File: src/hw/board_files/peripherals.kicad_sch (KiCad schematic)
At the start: 28 parts, among them J5 Molex 104031-0811, Q1 PMOS, U5 NHD-C0220BIZ-FSRGB, U6 NEO-M9N, U7 BQ27427, U8 SHT30-DIS

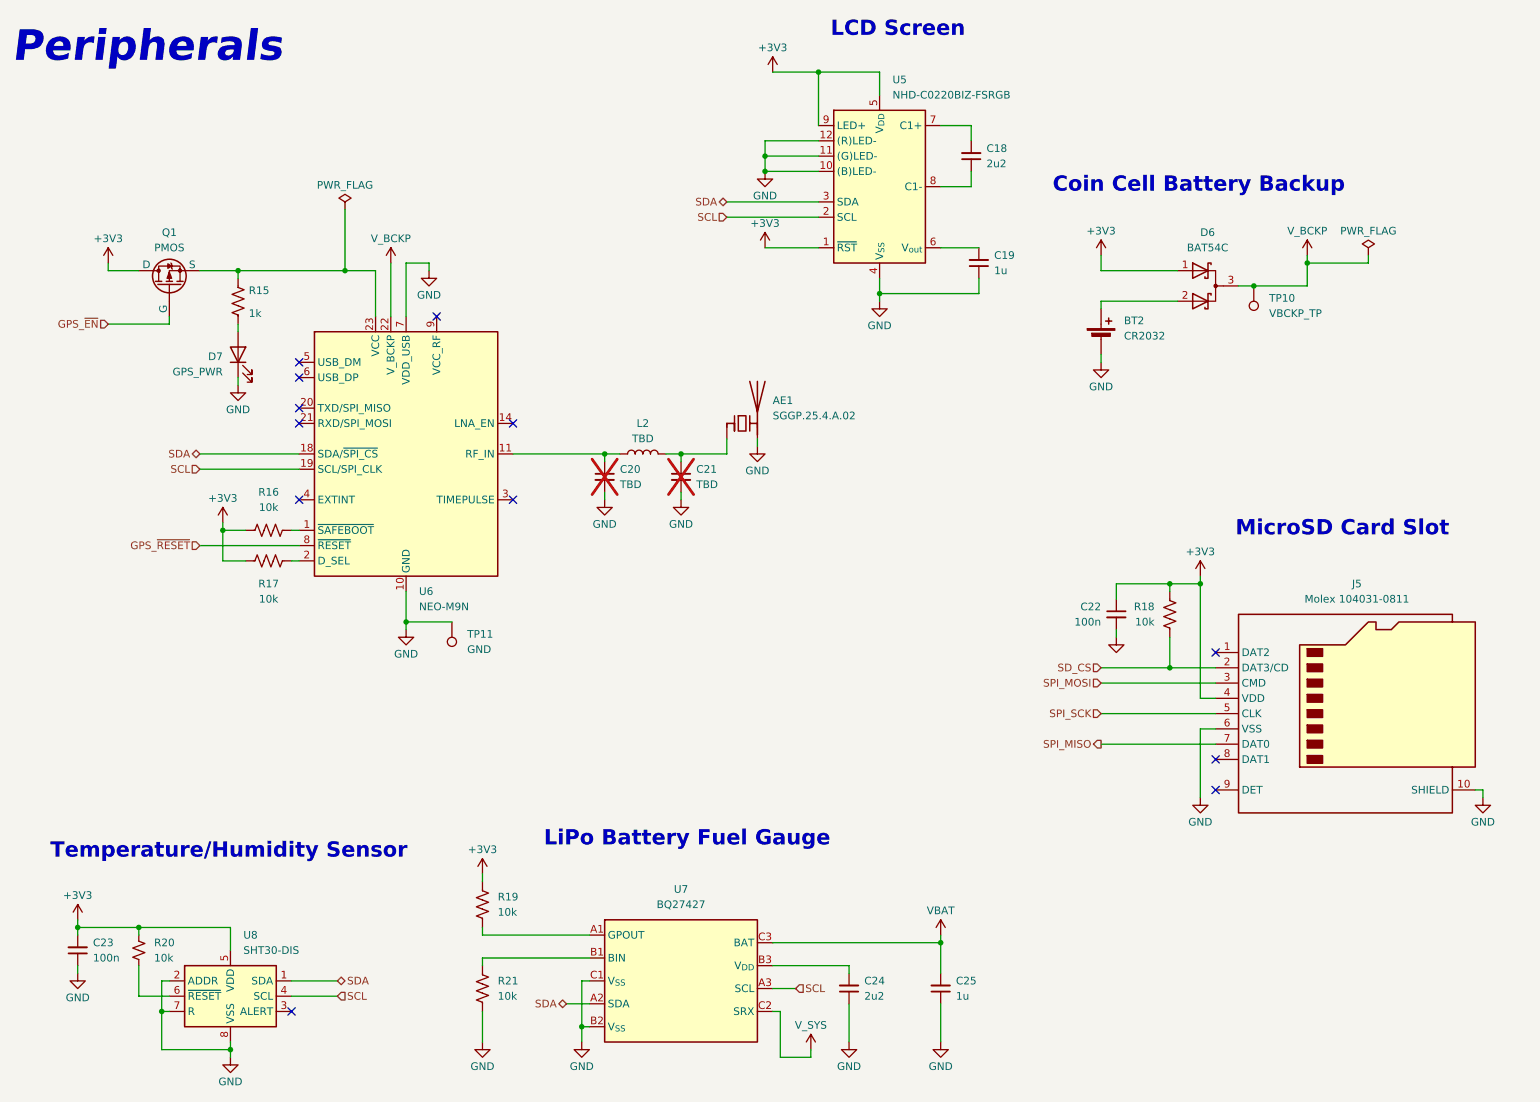
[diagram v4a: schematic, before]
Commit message: Lots of layout progress, changed some references (need to update BOM)
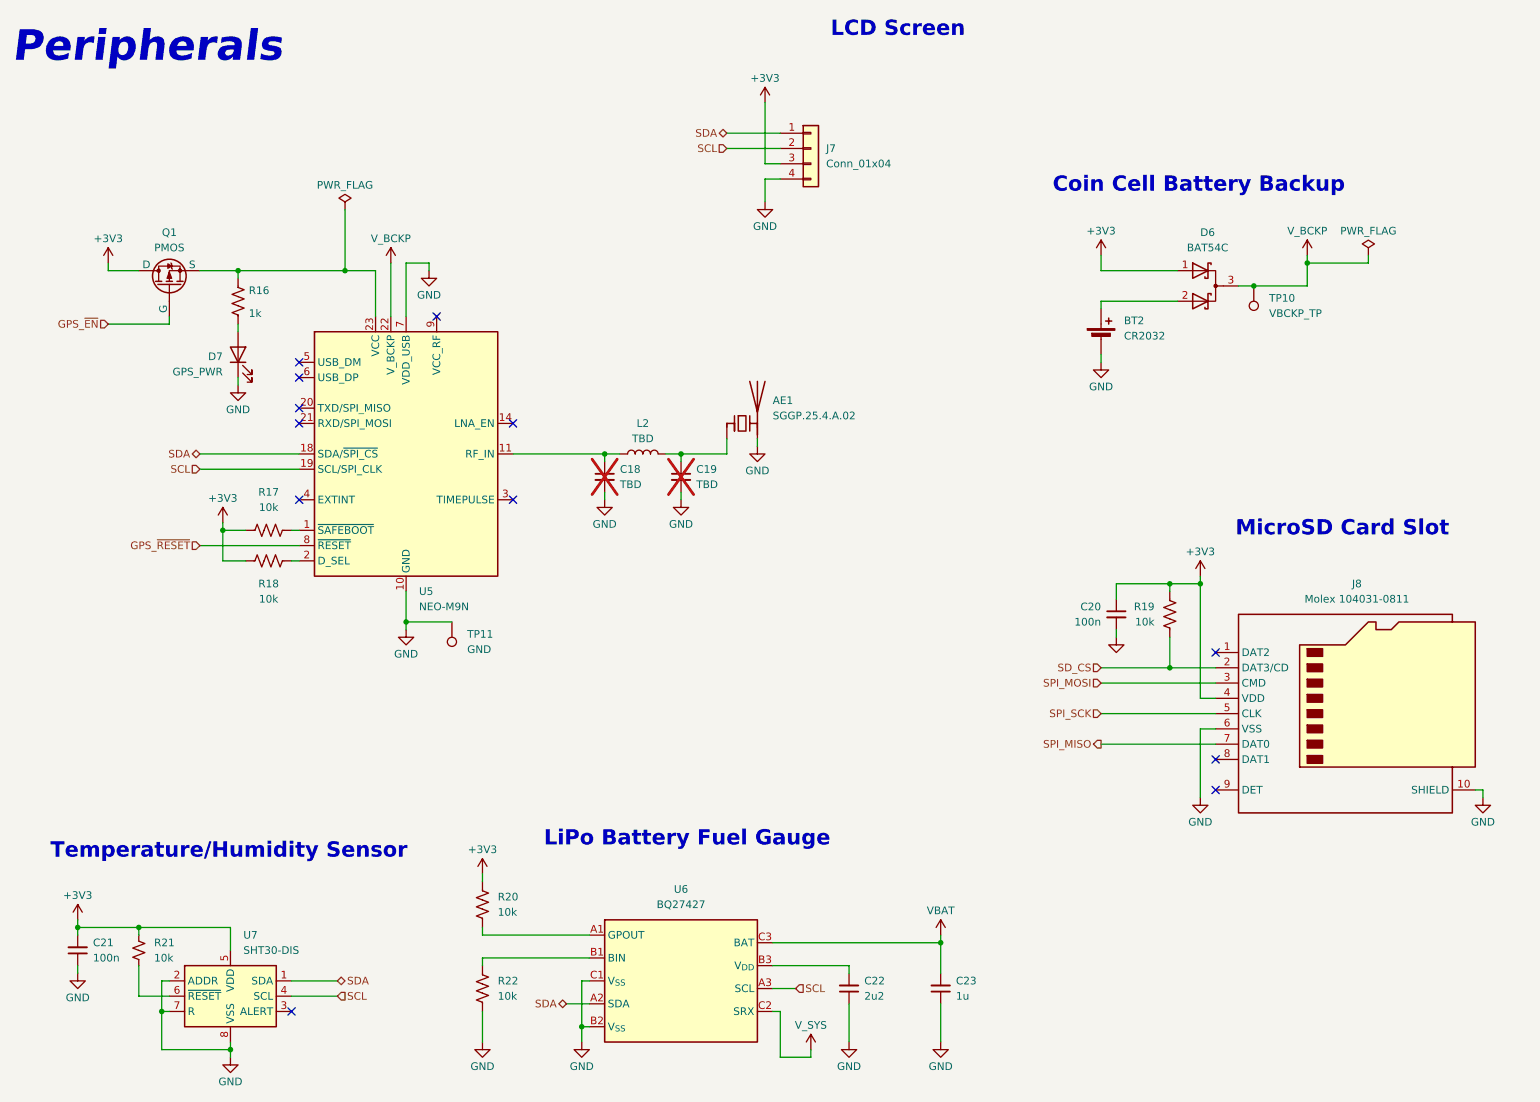
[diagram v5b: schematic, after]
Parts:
- removed C18: 2u2, Capacitor_SMD:C_0603_1608Metric_Pad1.08x0.95mm_HandSolder, symbol Device:C_Small
- removed C19: 1u, Capacitor_SMD:C_0603_1608Metric_Pad1.08x0.95mm_HandSolder, symbol Device:C_Small
- removed U5: NHD-C0220BIZ-FSRGB, Display:NHD-C0220BiZ-FSRGB, symbol Display_Character:NHD-C0220BIZ-FSRGB
- added J7: Conn_01x04, Connector_PinSocket_2.54mm:PinSocket_1x04_P2.54mm_Vertical, symbol Connector_Generic:Conn_01x04
- renumbered C20 to C18, C21 to C19, C22 to C20, C23 to C21, C24 to C22, C25 to C23, J5 to J8, R15 to R16, R16 to R17, R17 to R18, R18 to R19, R19 to R20, R20 to R21, R21 to R22, U6 to U5, U7 to U6, U8 to U7
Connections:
- net +3V3: now also J7.3 (Pin_3)
- net GND: now also J7.4 (Pin_4)
- net SCL: now also J7.2 (Pin_2)
- net SDA: now also J7.1 (Pin_1)

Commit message: Minor schematic updates
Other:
- note added: "OLED Screen"
- note removed: "LCD Screen"
- moved on the sheet: BT2, C20, C21, C22, C23, D6, J7, J8, R19, R20, R21, R22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

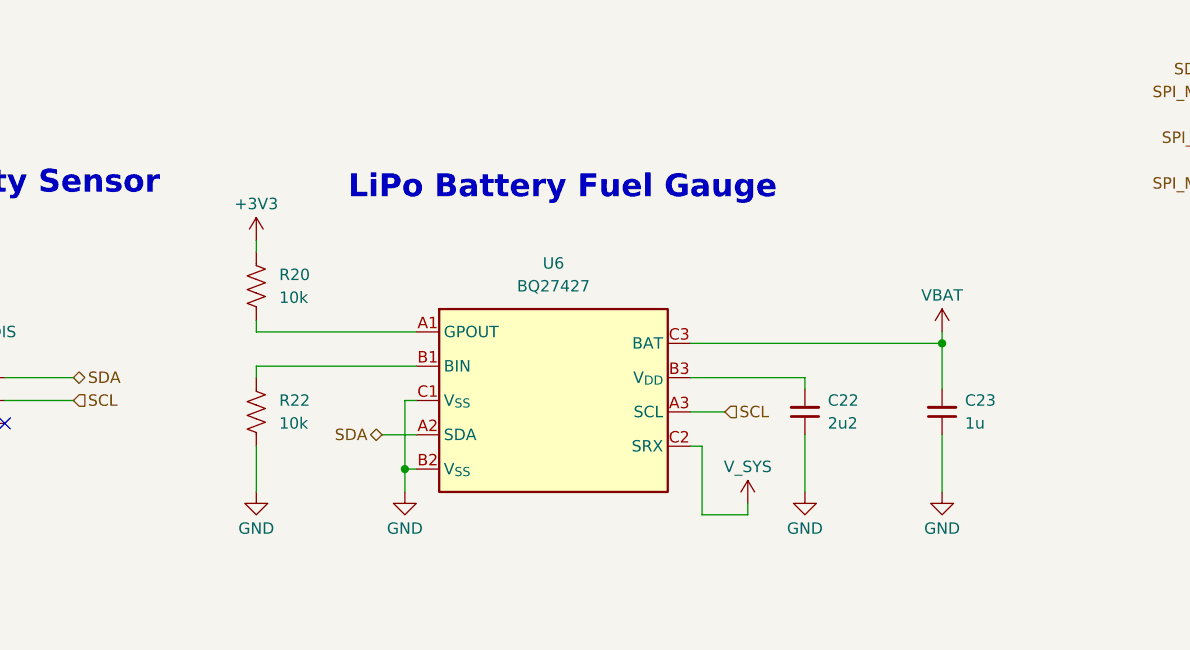
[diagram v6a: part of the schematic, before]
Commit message: Changed fuel gauge IC. Need to update component references and BOM.
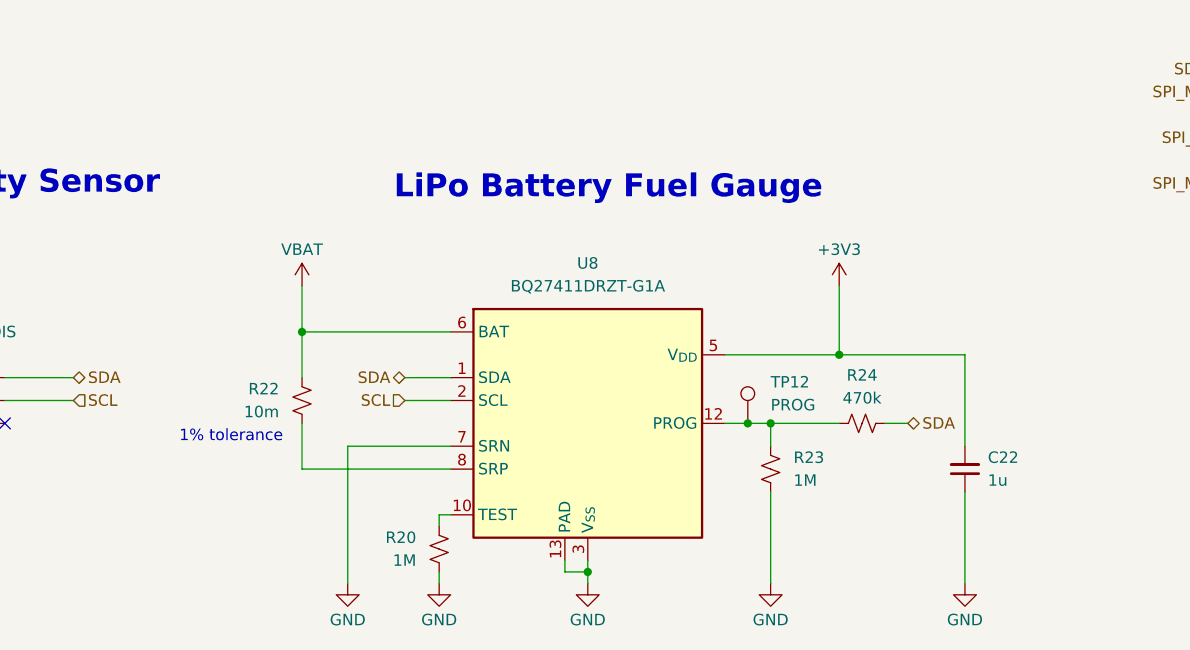
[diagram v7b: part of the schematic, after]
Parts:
- removed C23: 1u, Capacitor_SMD:C_0603_1608Metric_Pad1.08x0.95mm_HandSolder, symbol Device:C_Small
- removed R20, R22: 10k, Resistor_SMD:R_0603_1608Metric_Pad0.98x0.95mm_HandSolder, symbol Device:R_US
- removed U6: BQ27427, Package_BGA:Texas_DSBGA-9_1.62x1.58mm_Layout3x3_P0.5mm, symbol Project_Library:BQ27427
- added R20, R23: 1M, Resistor_SMD:R_0805_2012Metric_Pad1.20x1.40mm_HandSolder, symbol Device:R_Small_US
- added R22: 10m, Resistor_SMD:R_0603_1608Metric_Pad0.98x0.95mm_HandSolder, symbol Device:R_Small_US
- added R24: 470k, Resistor_SMD:R_0805_2012Metric_Pad1.20x1.40mm_HandSolder, symbol Device:R_Small_US
- added TP12: PROG, symbol Connector:TestPoint
- added U8: BQ27411DRZT-G1A, Package_SON:Texas_S-PDSO-N12, symbol Project_Library:BQ27411-G1
- C22: value 2u2 -> 1u
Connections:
- net +3V3: now also C22.2, U8.5 (V_{DD})
- net GND: now also R20.2, R23.1, U8.13 (PAD), U8.3 (V_{SS}), U8.7 (SRN)
- net SCL: now also U8.2 (SCL)
- net SDA: now also R24.1, U8.1 (SDA)
- net VBAT: now also R22.1, U8.6 (BAT)
- new net: R23.2, R24.2, TP12.1, U8.12 (PROG)
- new net: R20.1, U8.10 (TEST)
- new net: R22.2, U8.8 (SRP)
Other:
- note added: "1% tolerance"

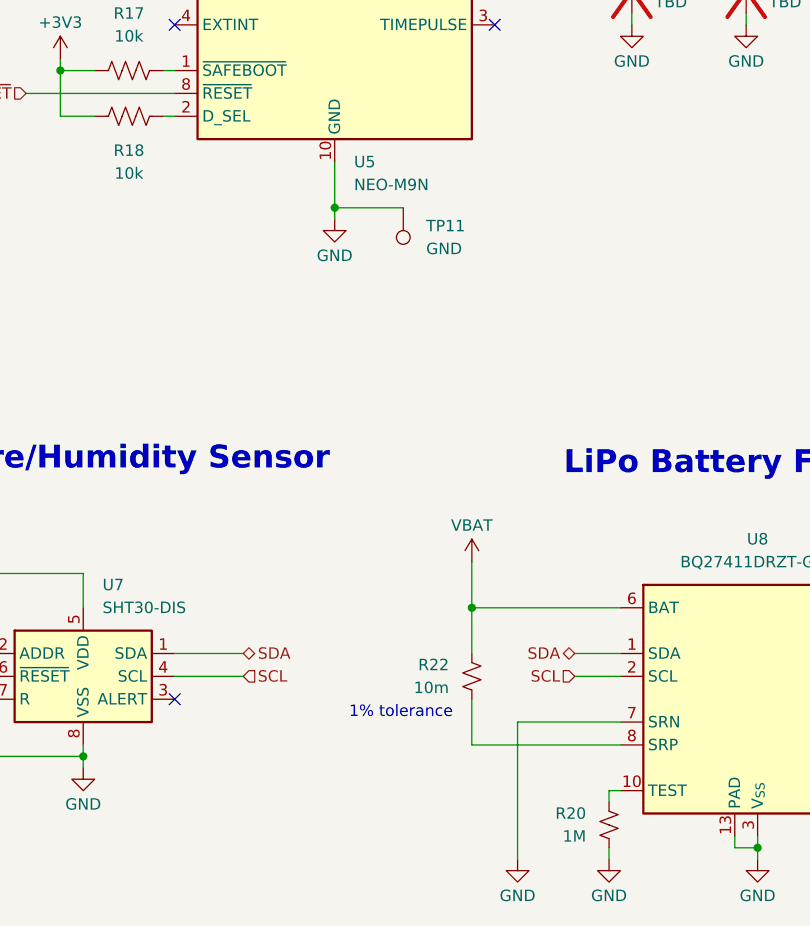
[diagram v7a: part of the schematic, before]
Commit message: Layout progress. Made new footprint for inductor. Changed test  points to pads
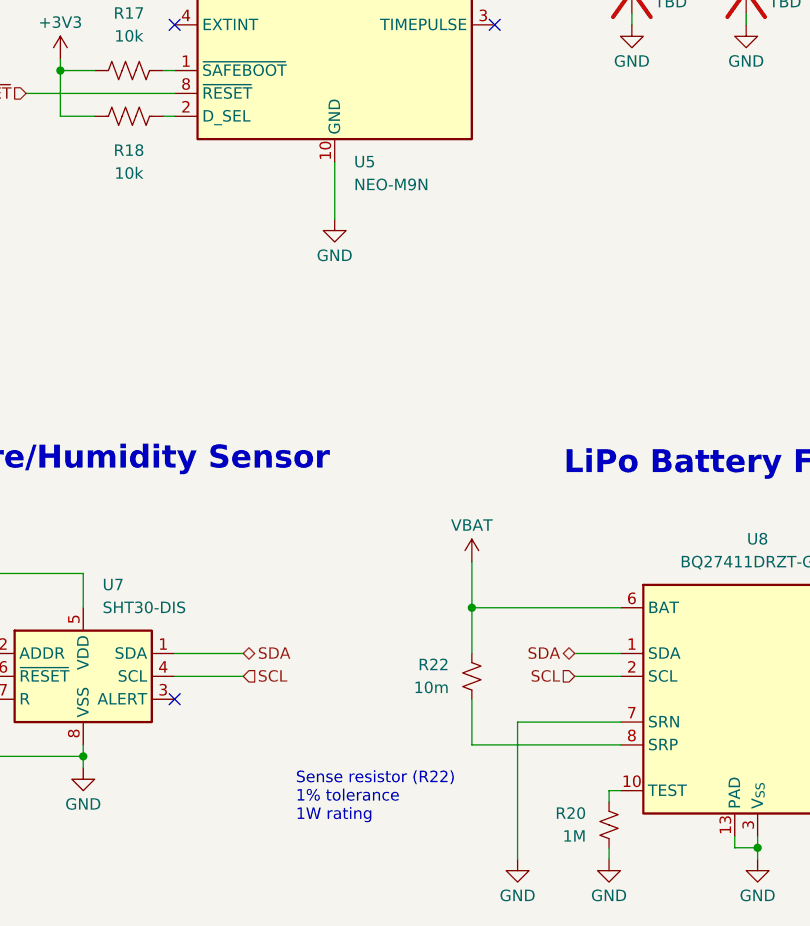
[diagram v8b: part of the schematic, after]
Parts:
- removed TP11: GND, TestPoint:TestPoint_Loop_D2.54mm_Drill1.5mm_Beaded, symbol Connector:TestPoint
- TP10: footprint TestPoint:TestPoint_Loop_D2.54mm_Drill1.5mm_Beaded -> TestPoint:TestPoint_Pad_D1.5mm; now left out of the parts list
- TP12: footprint (none) -> TestPoint:TestPoint_Pad_D1.5mm; now left out of the parts list
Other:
- note added: "Sense resistor (R22) 1% tolerance 1W rating"
- note removed: "1% tolerance"
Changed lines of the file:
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@@
 		(comment 2 "B. York")
 	)
-	(text "1% tolerance"
+	(text "Sense resistor (R22)\n1% tolerance\n1W rating"
 		(exclude_from_sim no)
-		(at 87.376 170.434 0)
+		(at 75.692 179.832 0)
 		(effects
 			(font
 				(size 1.27 1.27)
 			)
+			(justify left)
 		)
 	)
@@
 	)
 	(junction
-		(at 80.01 114.3)
-		(diameter 0)
-		(color 0 0 0 0)
-	)
-	(junction
 		(at 248.92 69.85)
 		(diameter 0)
@@
 	(wire
 		(pts
-			(xy 80.01 109.22) (xy 80.01 114.3)
+			(xy 80.01 109.22) (xy 80.01 115.57)
 		)
 		(stroke
@@
 	(wire
 		(pts
-			(xy 80.01 114.3) (xy 87.63 114.3)
-		)
-		(stroke
-			(width 0)
-			(type default)
-		)
-	)
-	(wire
-		(pts
 			(xy 168.91 161.29) (xy 154.94 161.29)
 		)
@@
 	(wire
 		(pts
-			(xy 80.01 114.3) (xy 80.01 115.57)
-		)
-		(stroke
-			(width 0)
-			(type default)
-		)
-	)
-	(wire
-		(pts
 			(xy 26.67 156.21) (xy 26.67 154.94)
 		)
@@
 		(unit 1)
 		(exclude_from_sim no)
-		(in_bom yes)
+		(in_bom no)
 		(on_board yes)
 		(dnp no)
@@
 			)
 		)
-		(property "Footprint" ""
+		(property "Footprint" "TestPoint:TestPoint_Pad_D1.5mm"
 			(at 149.86 168.91 0)
 			(effects
@@
 	)
 	(symbol
-		(lib_id "Connector:TestPoint")
-		(at 87.63 114.3 180)
-		(unit 1)
-		(exclude_from_sim no)
-		(in_bom yes)
-		(on_board yes)
-		(dnp no)
-		(fields_autoplaced yes)
-		(property "Reference" "TP11"
-			(at 90.17 116.3319 0)
-			(effects
-				(font
-					(size 1.27 1.27)
-				)
-				(justify right)
-			)
-		)
-		(property "Value" "GND"
-			(at 90.17 118.8719 0)
-			(effects
-				(font
-					(size 1.27 1.27)
-				)
-				(justify right)
-			)
-		)
-		(property "Footprint" "TestPoint:TestPoint_Loop_D2.54mm_Drill1.5mm_Beaded"
-			(at 82.55 114.3 0)
-			(effects
-				(font
-					(size 1.27 1.27)
-				)
-				(hide yes)
-			)
-		)
-		(property "Datasheet" "~"
-			(at 82.55 114.3 0)
-			(effects
-				(font
-					(size 1.27 1.27)
-				)
-				(hide yes)
-			)
-		)
-		(property "Description" "test point"
-			(at 87.63 114.3 0)
-			(effects
-				(font
-					(size 1.27 1.27)
-				)
-				(hide yes)
-			)
-		)
-		(pin "1"
-		)
-		(instances
-			(project "pocket-caddy"
-				(path "/2c77a8ba-b277-4959-adec-d3fc778c7960/81382524-b053-4c3c-9e13-c8b314c52639"
-					(reference "TP11")
-					(unit 1)
-				)
-			)
-		)
-	)
-	(symbol
 		(lib_id "power:GND")
 		(at 168.91 186.69 0)
@@
 		(unit 1)
 		(exclude_from_sim no)
-		(in_bom yes)
+		(in_bom no)
 		(on_board yes)
 		(dnp no)
@@
 			)
 		)
-		(property "Footprint" "TestPoint:TestPoint_Loop_D2.54mm_Drill1.5mm_Beaded"
+		(property "Footprint" "TestPoint:TestPoint_Pad_D1.5mm"
 			(at 234.95 73.66 0)
 			(effects
